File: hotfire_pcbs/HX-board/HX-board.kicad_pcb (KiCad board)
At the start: 2 copper layers, 101.5 x 88.5 mm, 54 parts, among them J1 Testpoints, J2 PCIE-LP-01-01-F-DV-A-TR, J3 DB15_Female, J4 Testpoints, J5 DB15_Female, J6 Testpoints, U1 HX711_Breakout, U2 HX711_Breakout, U3 HX711_Breakout, U4 HX711_Breakout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

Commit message: Updated HX711 Board
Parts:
- J6: value Testpoints -> PCIe_1
- moved JP5 159.8 mm to (148.8, 80.9), turned to -90 degrees
- moved JP18 156.6 mm to (144.6, 88.5), turned to 90 degrees
- moved JP10 152.7 mm to (154.2, 51.1), turned to 90 degrees
- moved JP7 151.0 mm to (144.3, 107.1), turned to -90 degrees
- moved JP11 149.9 mm to (159.3, 51.1), turned to 90 degrees
- moved JP3 146.3 mm to (149.1, 102.7), turned to 90 degrees
- moved R5 142.5 mm to (143.3, 46.3), turned to 90 degrees
- moved JP6 138.0 mm to (159.0, 102.7), turned to 90 degrees
- moved JP1 137.7 mm to (144.3, 102.5), turned to -90 degrees
- moved JP9 137.3 mm to (149.1, 107.3), turned to 90 degrees
- moved R16 137.1 mm to (144.2, 65.0), turned to 90 degrees
- moved R1 132.4 mm to (138.2, 119.0), turned to 90 degrees
- moved JP2 132.1 mm to (158.5, 96.6), turned to 90 degrees
- moved R10 131.1 mm to (143.5, 77.3), turned to -90 degrees
- moved R4 128.5 mm to (149.1, 97.4), turned to 90 degrees
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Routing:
- net GND: track 0.00 -> 402.0 mm, vias 0 -> 15
- net /HX_CLK: track 0.00 -> 205.3 mm, vias 0 -> 8
- net +5V: track 0.00 -> 187.1 mm, vias 0 -> 9
- net /PCIe_5: track 0.00 -> 101.2 mm, vias 0 -> 5
- net /PCIe_8: track 0.00 -> 99.4 mm
- net /PT3_A-: track 0.00 -> 96.8 mm, vias 0 -> 2
- net /PCIe_3: track 0.00 -> 96.1 mm, vias 0 -> 1
- net /PT3_E-: track 0.00 -> 90.5 mm, vias 0 -> 4
- net /PT5_E-: track 0.00 -> 86.3 mm, vias 0 -> 4
- net Net-(JP6-Pad1): track 0.00 -> 80.9 mm, vias 0 -> 2
- net /PT4_A-: track 0.00 -> 78.9 mm, vias 0 -> 4
- net /PT5_A-: track 0.00 -> 72.5 mm, vias 0 -> 8
- net /PT2_E-: track 0.00 -> 72.3 mm, vias 0 -> 3
- net /PT3_E+: track 0.00 -> 71.8 mm, vias 0 -> 4
- net /PT4_E-: track 0.00 -> 70.3 mm, vias 0 -> 4
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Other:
- board size 101.5 x 88.5 mm -> 101.6 x 88.5 mm

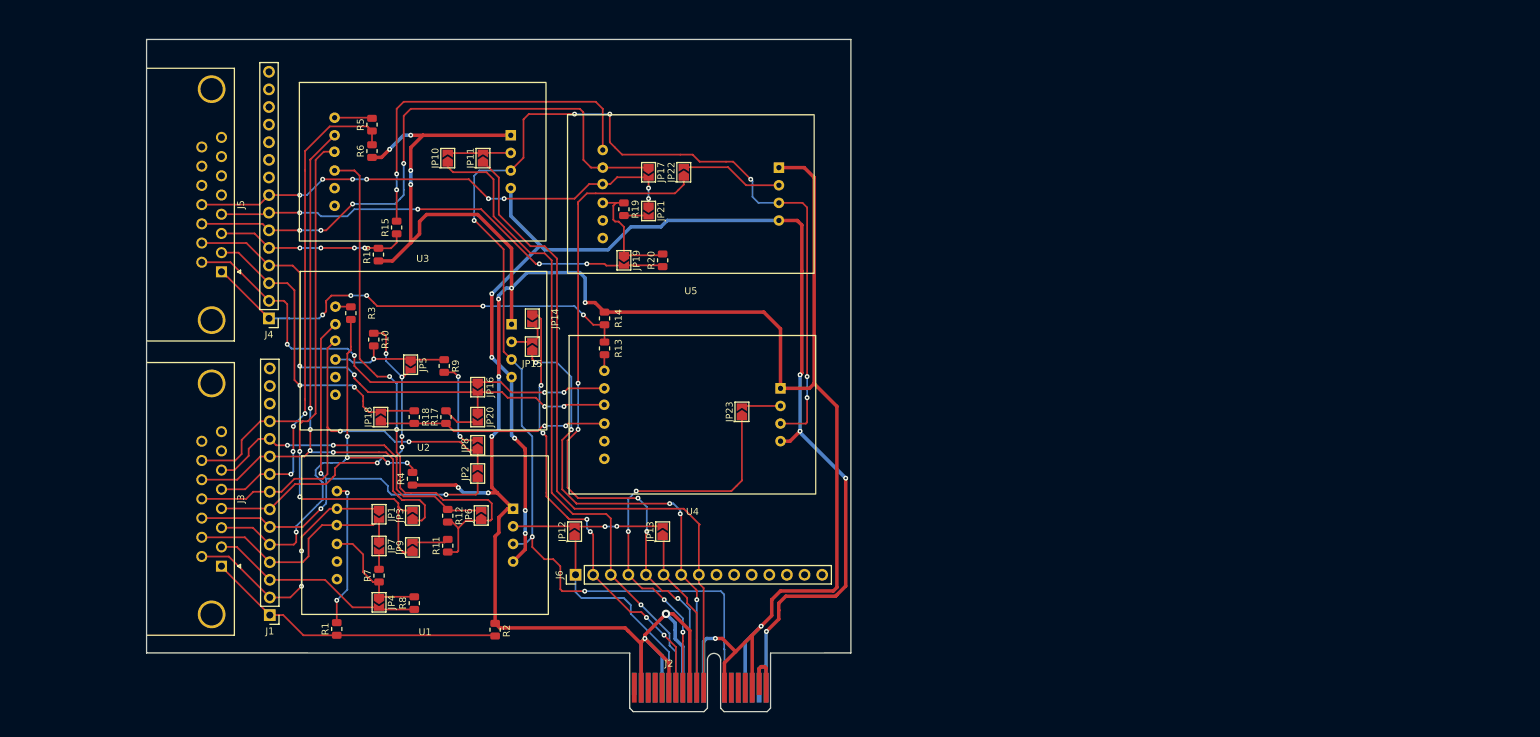
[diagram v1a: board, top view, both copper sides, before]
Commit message: Updated HX711
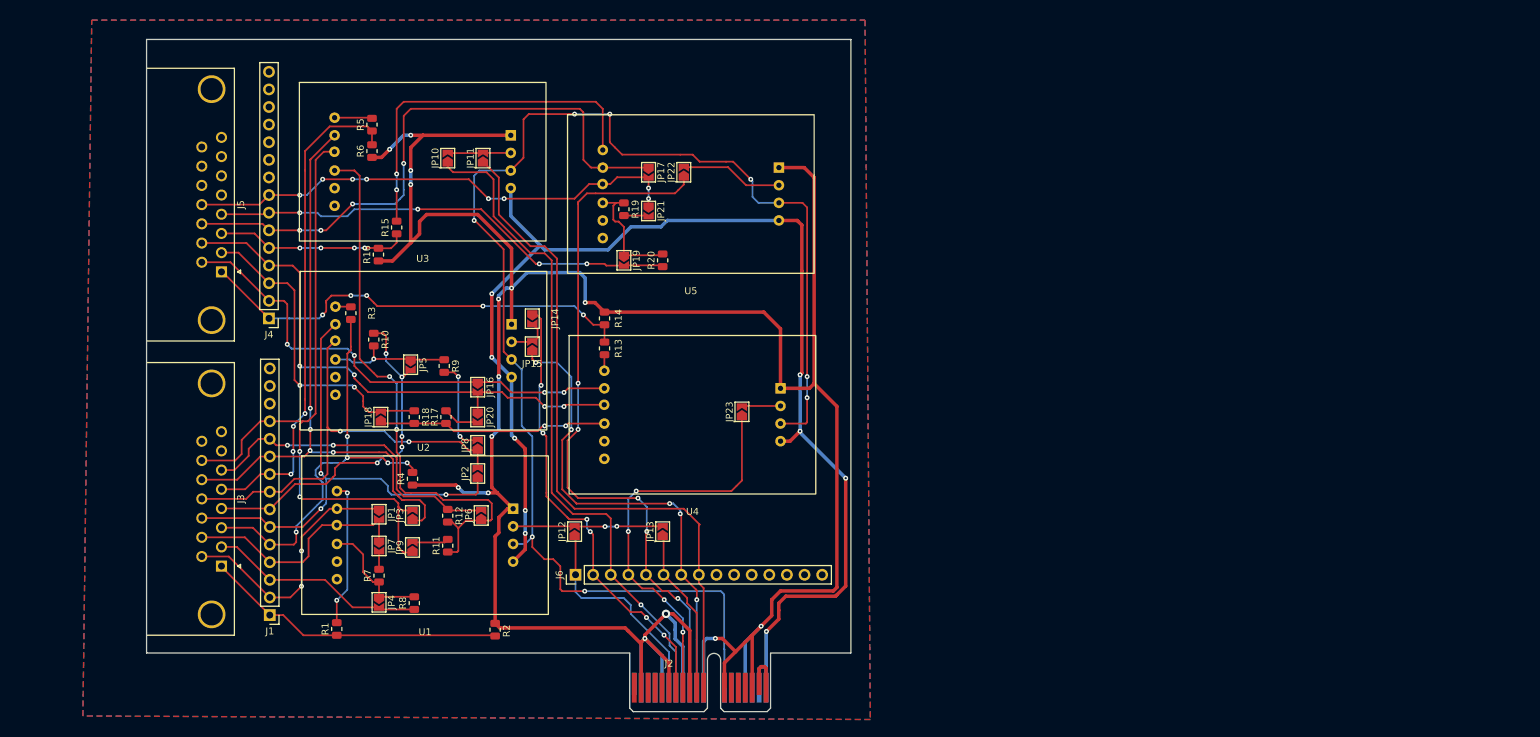
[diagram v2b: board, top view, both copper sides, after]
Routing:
- added copper zone on B.Cu, net GND
- added copper zone on F.Cu, net GND
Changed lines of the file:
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@@
   (via (at 146.836 55.708) (size 0.7112) (drill 0.3048) (layers "F.Cu" "B.Cu") (net 92))
   (segment (start 146.836 53.422) (end 146.836 55.708) (width 0.254) (layer "B.Cu") (net 92))
+  (zone (net 17) (net_name "GND") (layers F&B.Cu) (hatch edge 0.508)
+    (connect_pads (clearance 0.508))
+    (min_thickness 0.254) (filled_areas_thickness no)
+    (fill yes (thermal_gap 0.508) (thermal_bridge_width 0.508))
+    (polygon
+      (pts
+        (xy 215.138 132.08)
+        (xy 101.6 131.572)
+        (xy 102.87 31.242)
+        (xy 214.376 31.242)
+      )
+    )
+  )
 )

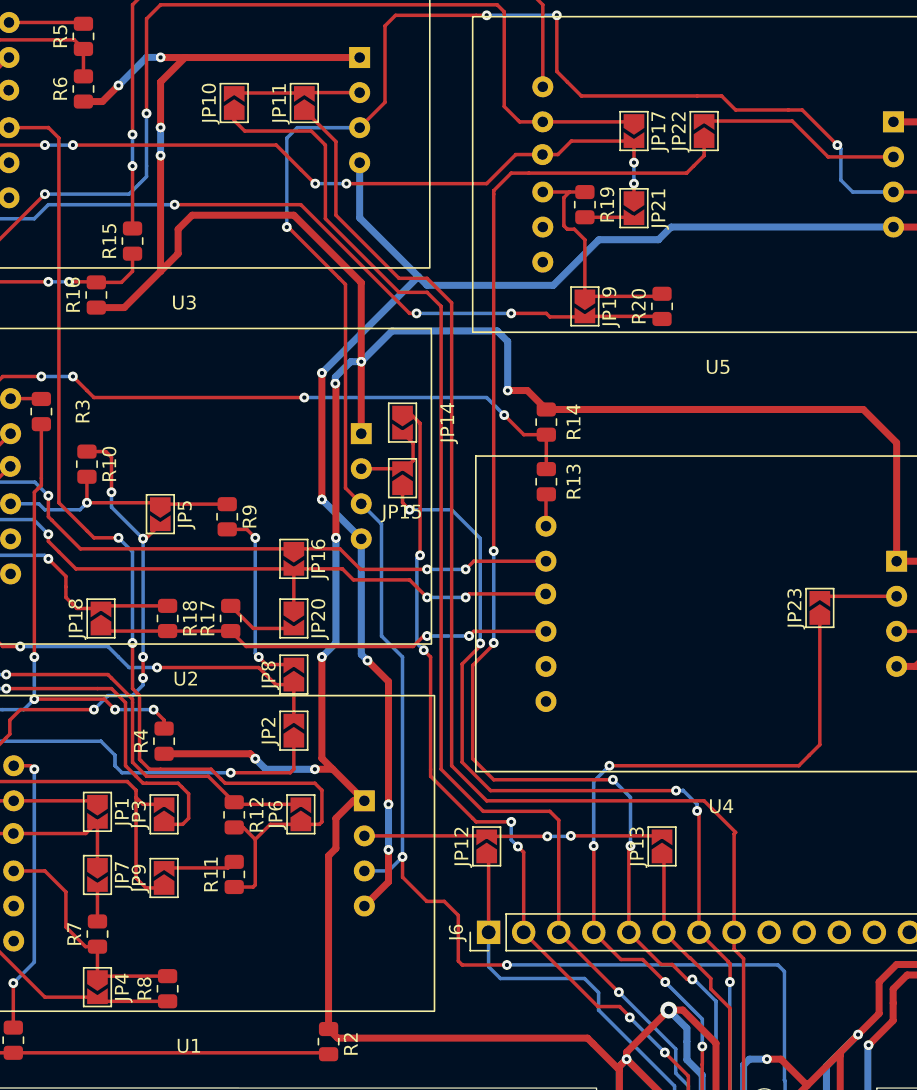
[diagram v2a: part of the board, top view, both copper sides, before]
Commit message: Changed solder jumper footprint to round pad.
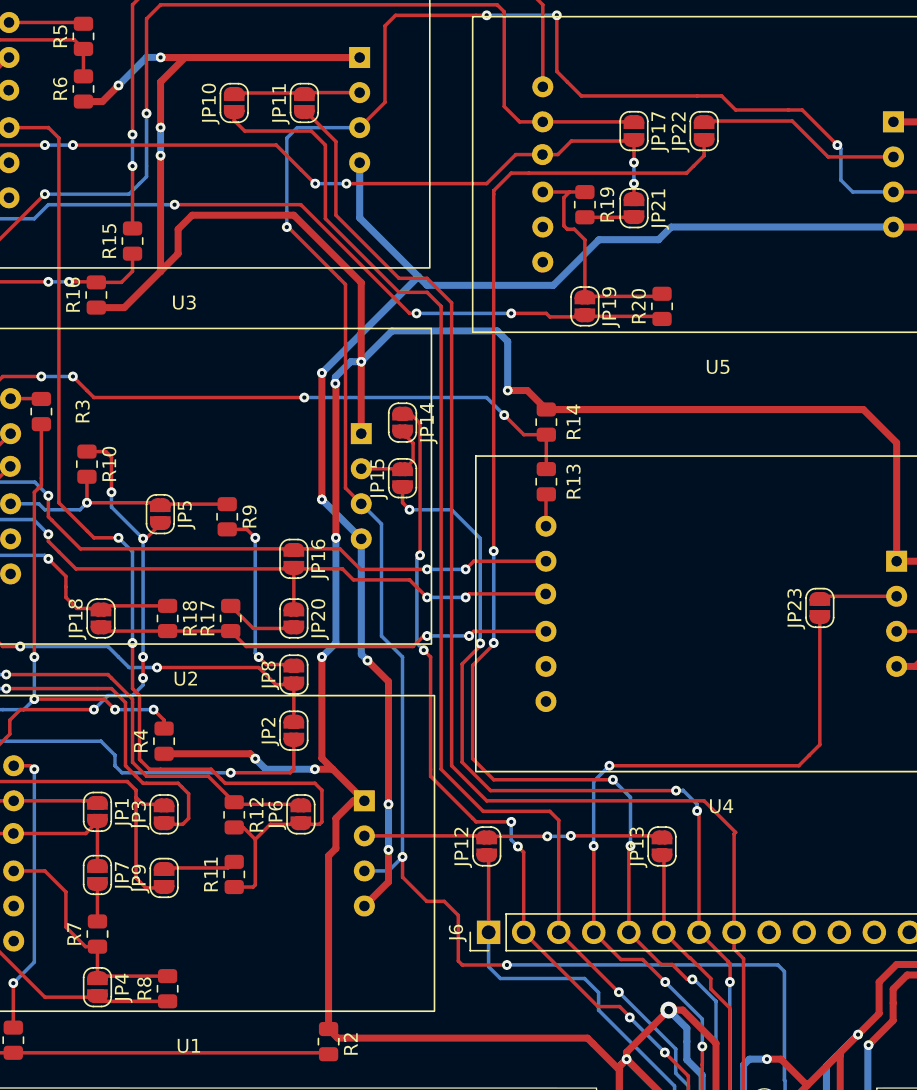
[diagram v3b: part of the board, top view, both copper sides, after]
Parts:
- J6: value PCIe_1 -> Testpoints
- JP1, JP10, JP11, JP12, JP13, JP14, JP15, JP16, JP17, JP18, JP19, JP2, JP20, JP21, JP22, JP23, JP3, JP4, JP5, JP6, JP7, JP8, JP9: footprint Jumper:SolderJumper-2_P1.3mm_Open_TrianglePad1.0x1.5mm -> Jumper:SolderJumper-2_P1.3mm_Open_RoundedPad1.0x1.5mm

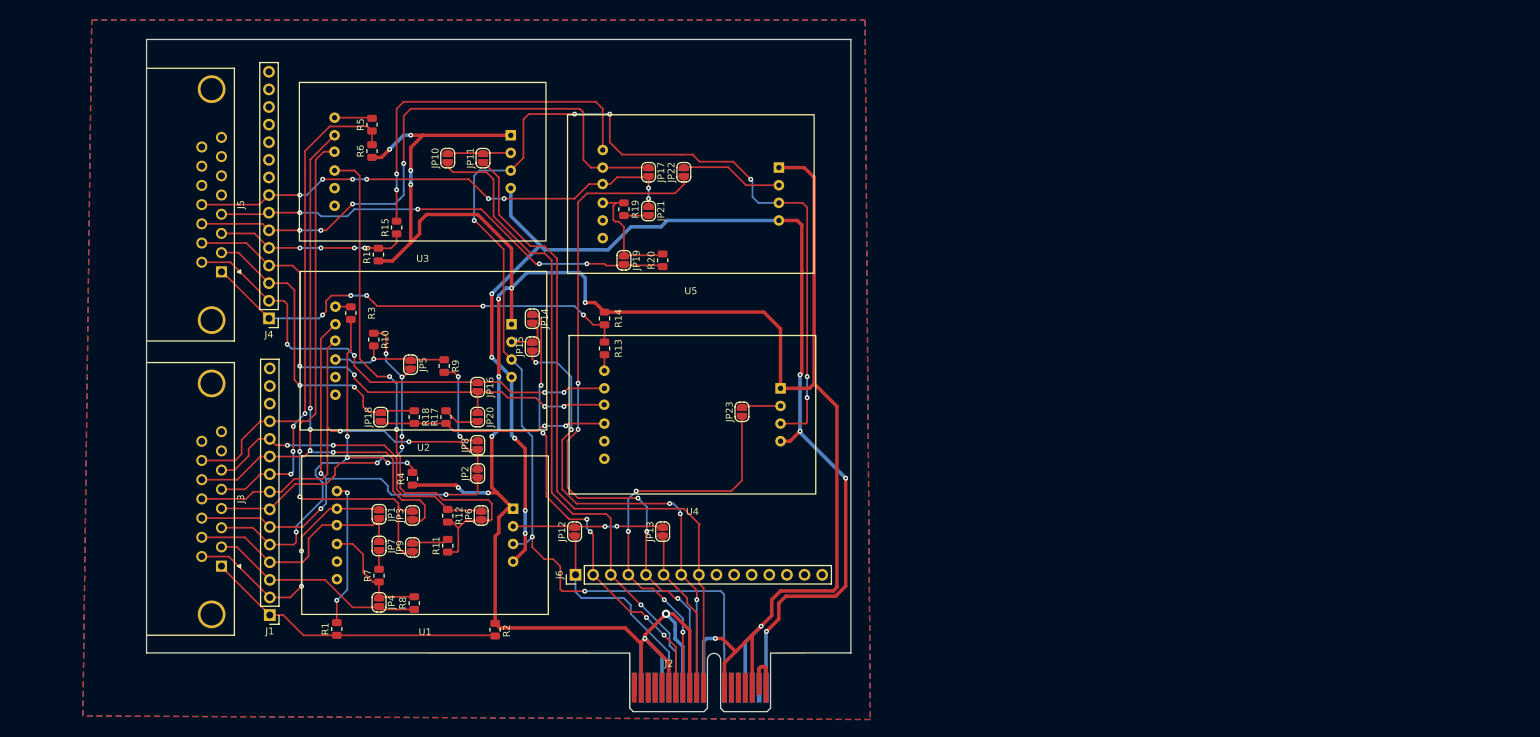
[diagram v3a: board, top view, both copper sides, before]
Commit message: Updated HX711
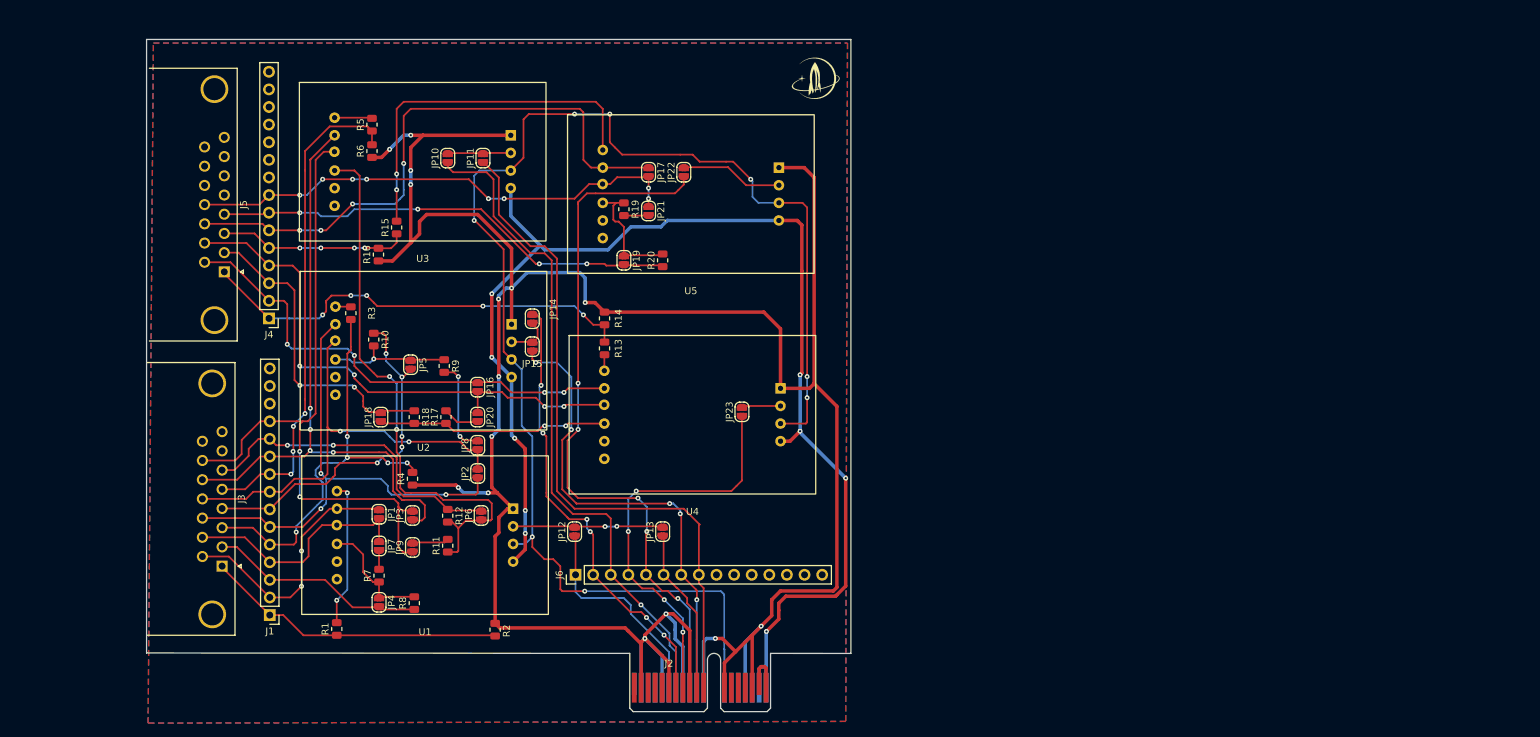
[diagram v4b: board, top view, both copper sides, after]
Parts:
- added G***: LOGO, star-common-lib:star_7x6, F.Cu at (207.3, 39.6)
- added G***: LOGO, LOGO, B.Cu at (198.6, 42.2)
- moved J5 0.41 mm to (122.0, 67.5)
- moved J3 0.09 mm to (121.7, 110.0)

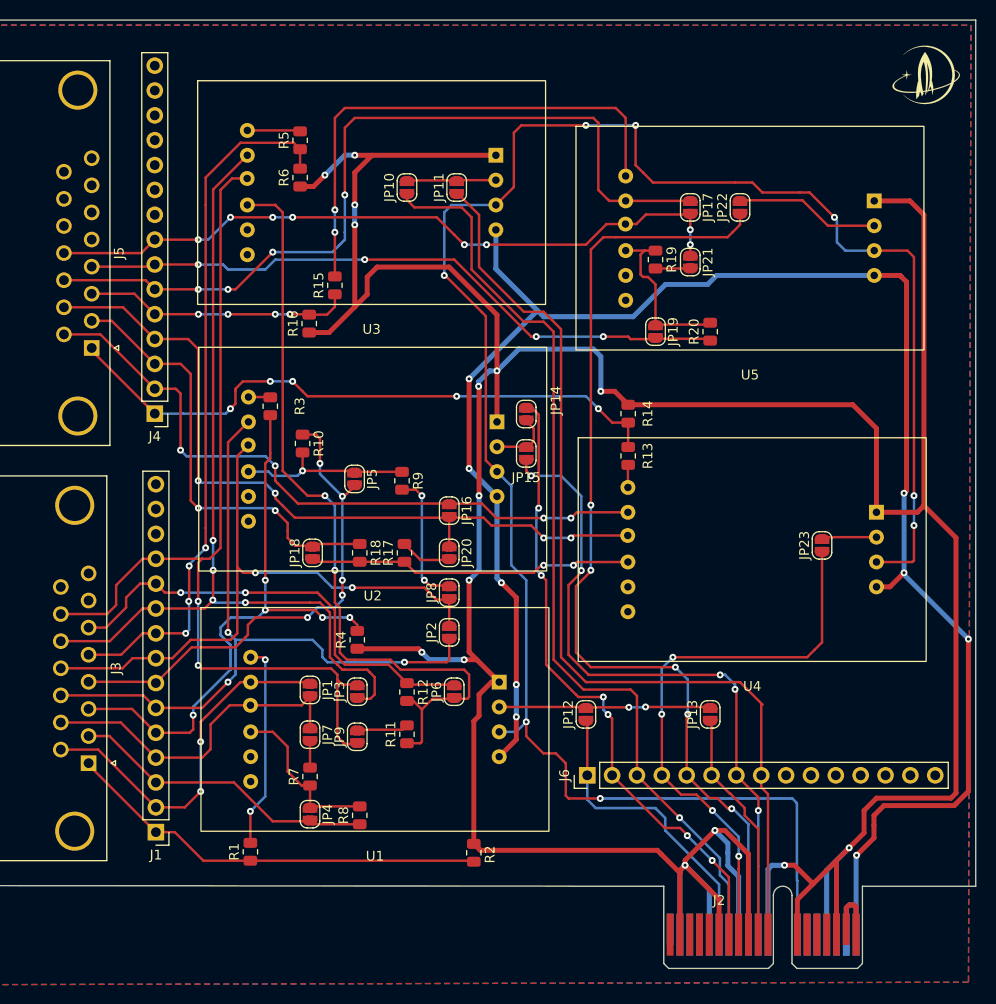
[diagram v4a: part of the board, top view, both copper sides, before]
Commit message: Revised components placement in layout.
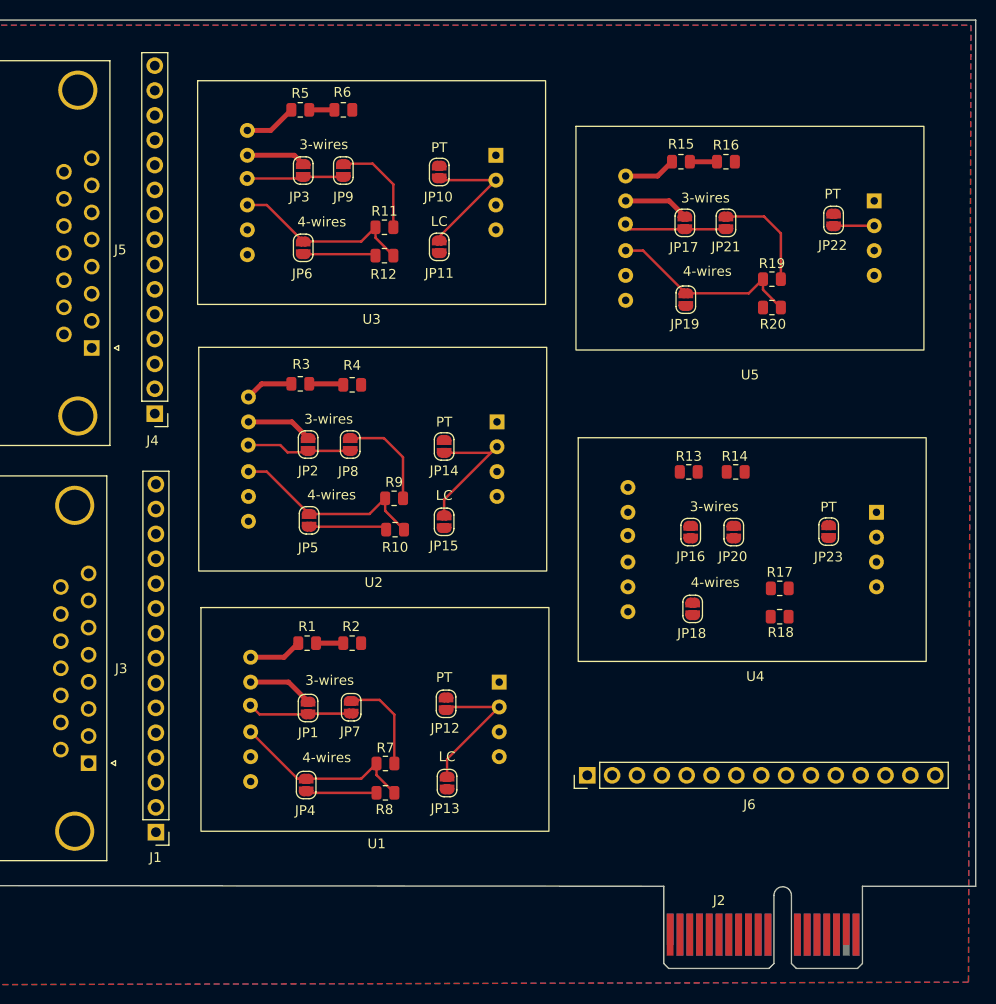
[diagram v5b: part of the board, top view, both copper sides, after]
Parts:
- removed the G*** at (207.3, 39.6)
- J2: footprint Connector_PCBEdge:BUS_PCIexpress_x1 -> PCIe_x1_card_edge:PCIe_x1_card_edge
- moved JP9 57.9 mm to (147.7, 49.4)
- moved JP3 53.5 mm to (143.6, 49.4), turned to -90 degrees
- moved R11 51.9 mm to (151.9, 55.2), turned to 0 degrees
- moved JP6 47.9 mm to (143.6, 57.3), turned to -90 degrees
- moved R16 45.7 mm to (186.8, 48.5), turned to 180 degrees
- moved R12 44.7 mm to (151.9, 58.1), turned to 0 degrees
- moved R18 43.4 mm to (192.3, 95.0), turned to 0 degrees
- moved JP18 39.3 mm to (183.4, 94.2), turned to -90 degrees
- moved R17 38.5 mm to (192.3, 92.1), turned to 0 degrees
- moved R15 37.6 mm to (182.2, 48.5), turned to 180 degrees
- moved JP20 29.2 mm to (187.6, 86.3), turned to 90 degrees
- moved JP13 27.8 mm to (158.3, 112.0)
- moved R4 26.1 mm to (148.6, 71.3), turned to 180 degrees
- moved JP16 24.8 mm to (183.2, 86.3)
- moved R2 24.8 mm to (148.6, 97.7), turned to 180 degrees
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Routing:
- net GND: track 402.0 -> 0.00 mm, vias 15 -> 0
- net /HX_CLK: track 205.3 -> 0.00 mm, vias 8 -> 0
- net +5V: track 187.1 -> 0.00 mm, vias 9 -> 0
- net /PCIe_5: track 101.2 -> 0.00 mm, vias 5 -> 0
- net /PCIe_8: track 99.4 -> 0.00 mm
- net /PCIe_3: track 96.1 -> 0.00 mm, vias 1 -> 0
- net /PT3_A-: track 96.8 -> 9.90 mm, vias 2 -> 0
- net /PT3_E-: track 90.5 -> 6.09 mm, vias 4 -> 0
- net /PT5_E-: track 86.2 -> 6.71 mm, vias 4 -> 0
- net /PT4_A-: track 78.9 -> 0.00 mm, vias 4 -> 0
- net /PT4_E-: track 70.3 -> 0.00 mm, vias 4 -> 0
- net /PCIe_7: track 69.4 -> 0.00 mm, vias 5 -> 0
- net /PT3_E+: track 71.8 -> 2.57 mm, vias 4 -> 0
- net /PT5_A+: track 67.8 -> 0.00 mm, vias 4 -> 0
- net /PT2_E-: track 72.3 -> 6.78 mm, vias 3 -> 0
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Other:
- board text added: "3-wires"
- board text added: "4-wires"
- board text added: "LC"
- board text added: "PT"
